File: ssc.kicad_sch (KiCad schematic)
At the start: 29 parts, among them J1 IRQ ENABLE, J2 RS-232 OUT, P1 A2Bus, U1 74HCT245, U2 28C256, U3 74HC00, U4 SSCGLU, U5 W65C51NxP, U6 MAX3232, U7 MAX3232, Y1 1.8432 MHz

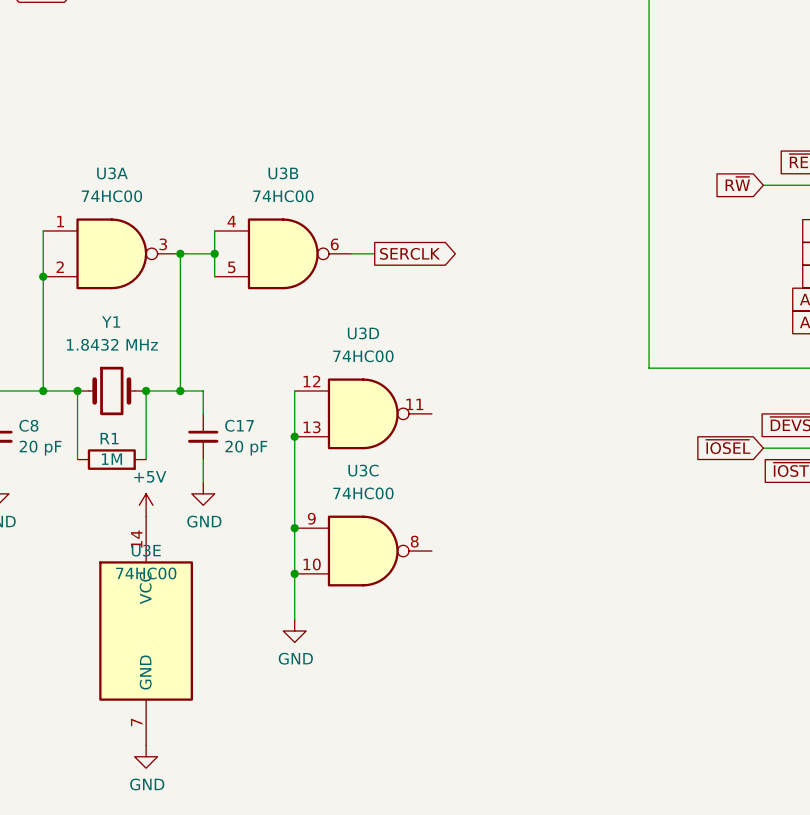
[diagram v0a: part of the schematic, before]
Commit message: Added NAND gate and labels
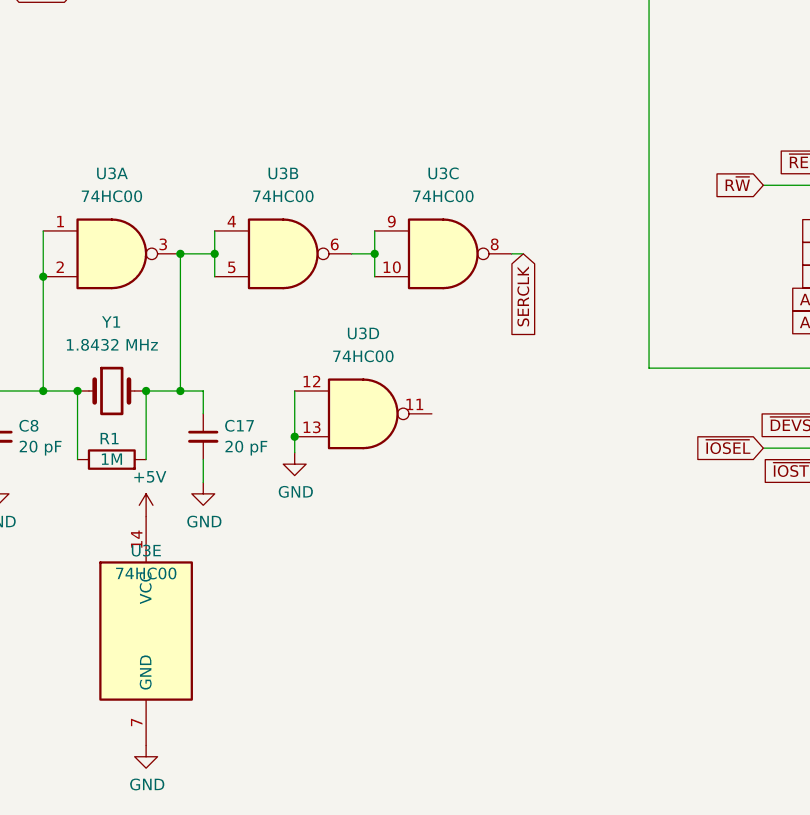
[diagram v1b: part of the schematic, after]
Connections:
- net GND: no longer U3.10, U3.9
- net SERCLK: now also U3.8; no longer U3.6
- new net: U3.10, U3.6, U3.9
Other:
- moved on the sheet: U3C
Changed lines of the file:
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@@
   (junction (at 87.63 223.52) (diameter 0) (color 0 0 0 0)
   )
-  (junction (at 100.33 243.84) (diameter 0) (color 0 0 0 0)
-  )
   (junction (at 91.44 208.28) (diameter 0) (color 0 0 0 0)
   )
@@
   (junction (at 87.63 208.28) (diameter 0) (color 0 0 0 0)
   )
-  (junction (at 100.33 238.76) (diameter 0) (color 0 0 0 0)
-  )
   (junction (at 129.54 113.03) (diameter 0) (color 0 0 0 0)
   )
@@
   )
   (junction (at 129.54 128.27) (diameter 0) (color 0 0 0 0)
+  )
+  (junction (at 109.22 208.28) (diameter 0) (color 0 0 0 0)
   )
   (junction (at 391.16 236.22) (diameter 0) (color 0 0 0 0)
@@
     (stroke (width 0) (type default) (color 0 0 0 0))
   )
+  (wire (pts (xy 109.22 205.74) (xy 109.22 208.28))
+    (stroke (width 0) (type default) (color 0 0 0 0))
+  )
   (wire (pts (xy 71.12 106.68) (xy 66.04 106.68))
     (stroke (width 0) (type default) (color 0 0 0 0))
   )
+  (wire (pts (xy 124.46 208.28) (xy 125.73 208.28))
+    (stroke (width 0) (type default) (color 0 0 0 0))
+  )
   (wire (pts (xy 313.69 55.88) (xy 369.57 55.88))
     (stroke (width 0) (type default) (color 0 0 0 0))
@@
     (stroke (width 0) (type default) (color 0 0 0 0))
   )
-  (wire (pts (xy 100.33 243.84) (xy 100.33 248.92))
+  (wire (pts (xy 100.33 228.6) (xy 100.33 230.378))
     (stroke (width 0) (type default) (color 0 0 0 0))
   )
@@
     (stroke (width 0) (type default) (color 0 0 0 0))
   )
-  (wire (pts (xy 100.33 238.76) (xy 100.33 243.84))
-    (stroke (width 0) (type default) (color 0 0 0 0))
-  )
   (wire (pts (xy 320.04 130.81) (xy 320.04 129.54))
     (stroke (width 0) (type default) (color 0 0 0 0))
@@
     (stroke (width 0) (type default) (color 0 0 0 0))
   )
-  (wire (pts (xy 100.33 228.6) (xy 100.33 238.76))
-    (stroke (width 0) (type default) (color 0 0 0 0))
-  )
   (wire (pts (xy 71.12 138.43) (xy 71.12 106.68))
     (stroke (width 0) (type default) (color 0 0 0 0))
@@
     (stroke (width 0) (type default) (color 0 0 0 0))
   )
+  (wire (pts (xy 106.68 208.28) (xy 109.22 208.28))
+    (stroke (width 0) (type default) (color 0 0 0 0))
+  )
   (wire (pts (xy 135.89 113.03) (xy 129.54 113.03))
     (stroke (width 0) (type default) (color 0 0 0 0))
@@
     (stroke (width 0) (type default) (color 0 0 0 0))
   )
+  (wire (pts (xy 109.22 208.28) (xy 109.22 210.82))
+    (stroke (width 0) (type default) (color 0 0 0 0))
+  )
   (wire (pts (xy 139.7 163.83) (xy 243.84 163.83))
     (stroke (width 0) (type default) (color 0 0 0 0))
@@
     (stroke (width 0) (type default) (color 0 0 0 0))
   )
-  (wire (pts (xy 106.68 208.28) (xy 109.22 208.28))
-    (stroke (width 0) (type default) (color 0 0 0 0))
-  )
   (wire (pts (xy 336.55 73.66) (xy 336.55 104.14))
     (stroke (width 0) (type default) (color 0 0 0 0))
@@
     )
   )
-  (global_label "SERCLK" (shape output) (at 109.22 208.28 0) (fields_autoplaced)
-    (effects (font (size 1.27 1.27)) (justify left))
-    (property "Intersheet References" "${INTERSHEET_REFS}" (id 0) (at 33.02 -39.37 0)
-      (effects (font (size 1.27 1.27)) hide)
-    )
-  )
   (global_label "D6" (shape bidirectional) (at 33.02 163.83 180) (fields_autoplaced)
     (effects (font (size 1.27 1.27)) (justify right))
@@
     (property "Intersheet References" "${INTERSHEET_REFS}" (id 0) (at 0 0 0)
       (effects (font (size 1.27 1.27)) hide)
+    )
+  )
+  (global_label "SERCLK" (shape input) (at 125.73 208.28 270) (fields_autoplaced)
+    (effects (font (size 1.27 1.27)) (justify right))
+    (property "Intersheet References" "${INTERSHEET_REFS}" (id 0) (at 125.6506 217.8009 90)
+      (effects (font (size 1.27 1.27)) (justify right) hide)
     )
   )
@@
   )
   (symbol (lib_id "74xx:74HC00") (at 99.06 208.28 0) (unit 2)
-    (in_bom yes) (on_board yes) (fields_autoplaced)
+    (in_bom yes) (on_board yes)
     (property "Reference" "U3" (id 0) (at 99.06 199.39 0))
     (property "Value" "74HC00" (id 1) (at 99.06 201.93 0))
@@
     (pin "2")
   )
-  (symbol (lib_id "74xx:74HC00") (at 107.95 241.3 0) (unit 3)
+  (symbol (lib_id "74xx:74HC00") (at 116.84 208.28 0) (unit 3)
     (in_bom yes) (on_board yes) (fields_autoplaced)
-    (property "Reference" "U3" (id 0) (at 107.95 232.41 0))
-    (property "Value" "74HC00" (id 1) (at 107.95 234.95 0))
-    (property "Footprint" "Package_DIP:DIP-14_W7.62mm_Socket" (id 2) (at 107.95 241.3 0)
-      (effects (font (size 1.27 1.27)) hide)
-    )
-    (property "Datasheet" "http://www.ti.com/lit/gpn/sn74hc00" (id 3) (at 107.95 241.3 0)
+    (property "Reference" "U3" (id 0) (at 116.84 199.39 0))
+    (property "Value" "74HC00" (id 1) (at 116.84 201.93 0))
+    (property "Footprint" "Package_DIP:DIP-14_W7.62mm_Socket" (id 2) (at 116.84 208.28 0)
+      (effects (font (size 1.27 1.27)) hide)
+    )
+    (property "Datasheet" "http://www.ti.com/lit/gpn/sn74hc00" (id 3) (at 116.84 208.28 0)
       (effects (font (size 1.27 1.27)) hide)
     )
@@
     (pin "1")
   )
-  (symbol (lib_id "power:GND") (at 100.33 248.92 0) (unit 1)
-    (in_bom yes) (on_board yes)
-    (property "Reference" "#PWR0121" (id 0) (at 100.33 255.27 0)
-      (effects (font (size 1.27 1.27)) hide)
-    )
-    (property "Value" "GND" (id 1) (at 100.457 253.3142 0))
-    (property "Footprint" "" (id 2) (at 100.33 248.92 0)
-      (effects (font (size 1.27 1.27)) hide)
-    )
-    (property "Datasheet" "" (id 3) (at 100.33 248.92 0)
-      (effects (font (size 1.27 1.27)) hide)
-    )
+  (symbol (lib_id "power:GND") (at 100.33 230.378 0) (unit 1)
+    (in_bom yes) (on_board yes)
+    (property "Reference" "#PWR0121" (id 0) (at 100.33 236.728 0)
+      (effects (font (size 1.27 1.27)) hide)
+    )
+    (property "Value" "GND" (id 1) (at 100.457 234.7722 0))
+    (property "Footprint" "" (id 2) (at 100.33 230.378 0)
+      (effects (font (size 1.27 1.27)) hide)
+    )
+    (property "Datasheet" "" (id 3) (at 100.33 230.378 0)
+      (effects (font (size 1.27 1.27)) hide)
+    )
